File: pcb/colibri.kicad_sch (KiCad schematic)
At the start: 91 parts

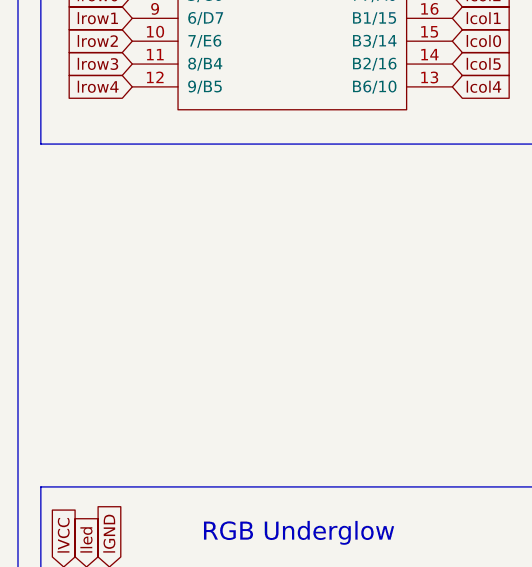
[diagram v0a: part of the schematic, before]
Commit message: TRRS jack in place
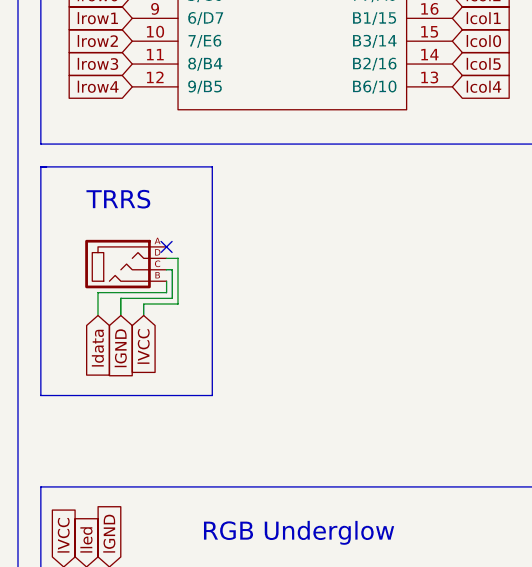
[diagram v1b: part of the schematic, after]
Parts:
- added ljack-1: MJ-4PP-9, kbd:MJ-4PP-9_1side, symbol kbd:MJ-4PP-9
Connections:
- net lGND: now also ljack-1.C
- net lVCC: now also ljack-1.D
- net ldata: now also ljack-1.B
- no-connect marks 7 -> 8
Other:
- note added: "TRRS"
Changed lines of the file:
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@@
   (no_connect (at 35.56 54.61))
   (no_connect (at 71.12 54.61))
+  (no_connect (at 39.37 90.17))
   (wire (pts (xy 163.83 78.74) (xy 163.83 91.44))
     (stroke (width 0) (type default) (color 0 0 0 0))
@@
     (stroke (width 0) (type default) (color 0 0 0 0))
   )
+  (wire (pts (xy 40.005 95.885) (xy 34.29 95.885))
+    (stroke (width 0) (type default) (color 0 0 0 0))
+  )
   (wire (pts (xy 130.81 53.34) (xy 130.81 66.04))
     (stroke (width 0) (type default) (color 0 0 0 0))
@@
     (stroke (width 0) (type default) (color 0 0 0 0))
   )
+  (wire (pts (xy 40.64 91.44) (xy 40.64 96.52))
+    (stroke (width 0) (type default) (color 0 0 0 0))
+  )
   (wire (pts (xy 154.94 68.58) (xy 154.94 72.39))
     (stroke (width 0) (type default) (color 0 0 0 0))
@@
   (wire (pts (xy 39.37 143.51) (xy 39.37 144.78))
     (stroke (width 0) (type default) (color 0 0 0 0))
+  )
+  (polyline (pts (xy 44.45 106.68) (xy 25.4 106.68))
+    (stroke (width 0) (type solid) (color 0 0 0 0))
   )
   (wire (pts (xy 177.8 149.86) (xy 177.8 165.1))
@@
     (stroke (width 0) (type solid) (color 0 0 0 0))
   )
+  (wire (pts (xy 40.64 96.52) (xy 36.83 96.52))
+    (stroke (width 0) (type default) (color 0 0 0 0))
+  )
   (wire (pts (xy 142.24 195.58) (xy 143.51 195.58))
     (stroke (width 0) (type default) (color 0 0 0 0))
   )
+  (polyline (pts (xy 25.4 81.28) (xy 44.45 81.28))
+    (stroke (width 0) (type solid) (color 0 0 0 0))
+  )
   (wire (pts (xy 179.07 66.04) (xy 179.07 68.58))
     (stroke (width 0) (type default) (color 0 0 0 0))
@@
     (stroke (width 0) (type default) (color 0 0 0 0))
   )
+  (wire (pts (xy 39.37 93.98) (xy 39.37 95.25))
+    (stroke (width 0) (type default) (color 0 0 0 0))
+  )
   (wire (pts (xy 171.45 59.69) (xy 187.96 59.69))
     (stroke (width 0) (type default) (color 0 0 0 0))
+  )
+  (polyline (pts (xy 44.45 81.28) (xy 44.45 106.68))
+    (stroke (width 0) (type solid) (color 0 0 0 0))
   )
   (wire (pts (xy 160.02 165.1) (xy 160.02 180.34))
@@
     (stroke (width 0) (type default) (color 0 0 0 0))
   )
+  (polyline (pts (xy 25.4 81.28) (xy 26.035 81.28))
+    (stroke (width 0) (type default) (color 0 0 0 0))
+  )
   (wire (pts (xy 138.43 72.39) (xy 154.94 72.39))
     (stroke (width 0) (type default) (color 0 0 0 0))
@@
     (stroke (width 0) (type solid) (color 0 0 0 0))
   )
+  (polyline (pts (xy 25.4 106.68) (xy 25.4 81.28))
+    (stroke (width 0) (type solid) (color 0 0 0 0))
+  )
   (polyline (pts (xy 85.09 33.02) (xy 85.09 114.3))
     (stroke (width 0) (type solid) (color 0 0 0 0))
@@
     (stroke (width 0) (type default) (color 0 0 0 0))
   )
+  (wire (pts (xy 34.29 95.885) (xy 34.29 97.79))
+    (stroke (width 0) (type default) (color 0 0 0 0))
+  )
   (wire (pts (xy 158.75 165.1) (xy 160.02 165.1))
     (stroke (width 0) (type default) (color 0 0 0 0))
@@
     (stroke (width 0) (type default) (color 0 0 0 0))
   )
+  (wire (pts (xy 39.37 91.44) (xy 40.64 91.44))
+    (stroke (width 0) (type default) (color 0 0 0 0))
+  )
   (wire (pts (xy 106.68 165.1) (xy 107.95 165.1))
     (stroke (width 0) (type default) (color 0 0 0 0))
@@
   )
   (wire (pts (xy 154.94 59.69) (xy 171.45 59.69))
+    (stroke (width 0) (type default) (color 0 0 0 0))
+  )
+  (wire (pts (xy 40.005 92.71) (xy 40.005 95.885))
     (stroke (width 0) (type default) (color 0 0 0 0))
   )
@@
     (stroke (width 0) (type default) (color 0 0 0 0))
   )
+  (wire (pts (xy 31.75 95.25) (xy 31.75 97.79))
+    (stroke (width 0) (type default) (color 0 0 0 0))
+  )
   (wire (pts (xy 124.46 149.86) (xy 125.73 149.86))
     (stroke (width 0) (type default) (color 0 0 0 0))
@@
     (stroke (width 0) (type default) (color 0 0 0 0))
   )
+  (wire (pts (xy 39.37 95.25) (xy 31.75 95.25))
+    (stroke (width 0) (type default) (color 0 0 0 0))
+  )
   (wire (pts (xy 123.19 180.34) (xy 124.46 180.34))
     (stroke (width 0) (type default) (color 0 0 0 0))
   )
   (wire (pts (xy 171.45 68.58) (xy 171.45 72.39))
+    (stroke (width 0) (type default) (color 0 0 0 0))
+  )
+  (wire (pts (xy 39.37 92.71) (xy 40.005 92.71))
     (stroke (width 0) (type default) (color 0 0 0 0))
   )
@@
     (stroke (width 0) (type default) (color 0 0 0 0))
   )
+  (wire (pts (xy 36.83 96.52) (xy 36.83 97.79))
+    (stroke (width 0) (type default) (color 0 0 0 0))
+  )
   (wire (pts (xy 39.37 144.78) (xy 39.37 146.05))
     (stroke (width 0) (type default) (color 0 0 0 0))
@@
   (wire (pts (xy 130.81 91.44) (xy 130.81 104.14))
     (stroke (width 0) (type default) (color 0 0 0 0))
+  )
+  (text "TRRS" (at 30.48 86.36 0)
+    (effects (font (size 2 2)) (justify left bottom))
   )
   (text "SWITCHES" (at 134.62 38.1 0)
@@
     )
   )
+  (global_label "lVCC" (shape input) (at 36.83 97.79 270) (fields_autoplaced)
+    (effects (font (size 1.27 1.27)) (justify right))
+    (property "Intersheet References" "${INTERSHEET_REFS}" (id 0) (at 36.9094 104.4969 90)
+      (effects (font (size 1.27 1.27)) (justify right) hide)
+    )
+  )
   (global_label "lVCC" (shape input) (at 160.02 127 90) (fields_autoplaced)
     (effects (font (size 1.27 1.27)) (justify left))
@@
     )
   )
+  (global_label "ldata" (shape input) (at 31.75 97.79 270) (fields_autoplaced)
+    (effects (font (size 1.27 1.27)) (justify right))
+    (property "Intersheet References" "${INTERSHEET_REFS}" (id 0) (at 31.6706 105.0412 90)
+      (effects (font (size 1.27 1.27)) (justify right) hide)
+    )
+  )
   (global_label "lcol2" (shape input) (at 130.81 46.99 90) (fields_autoplaced)
     (effects (font (size 1.27 1.27)) (justify left))
@@
     )
   )
+  (global_label "lGND" (shape input) (at 34.29 97.79 270) (fields_autoplaced)
+    (effects (font (size 1.27 1.27)) (justify right))
+    (property "Intersheet References" "${INTERSHEET_REFS}" (id 0) (at 34.2106 104.7388 90)
+      (effects (font (size 1.27 1.27)) (justify right) hide)
+    )
+  )
   (global_label "lcol4" (shape input) (at 71.12 72.39 0) (fields_autoplaced)
     (effects (font (size 1.27 1.27)) (justify left))
@@
     (pin "1")
     (pin "2")
+  )
+  (symbol (lib_id "kbd:MJ-4PP-9") (at 34.29 92.075 0) (unit 1)
+    (in_bom yes) (on_board yes)
+    (property "Reference" "ljack-1" (id 0) (at 38.1 87.63 0)
+      (effects (font (size 1.27 1.27)) (justify right) hide)
+    )
+    (property "Value" "MJ-4PP-9" (id 1) (at 33.9725 86.995 0)
+      (effects (font (size 1.27 1.27)) hide)
+    )
+    (property "Footprint" "kbd:MJ-4PP-9_1side" (id 2) (at 41.275 87.63 0)
+      (effects (font (size 1.27 1.27)) hide)
+    )
+    (property "Datasheet" "~" (id 3) (at 41.275 87.63 0)
+      (effects (font (size 1.27 1.27)) hide)
+    )
+    (pin "A")
+    (pin "B")
+    (pin "C")
+    (pin "D")
   )
   (symbol (lib_id "kbd:SW_PUSH") (at 171.45 91.44 0) (unit 1)
@@
       (reference "ld-28") (unit 1) (value "1N4148W") (footprint "kbd:D3_SMD_v2")
     )
+    (path "/17a58034-d3db-4b2b-a530-114b7d872836"
+      (reference "ljack-1") (unit 1) (value "MJ-4PP-9") (footprint "kbd:MJ-4PP-9_1side")
+    )
     (path "/c8613400-5414-468d-9229-e822c0f7d70d"

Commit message: reset button
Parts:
- added lreset-1: SW_PUSH, kbd:ResetSW_4P, symbol kbd:SW_PUSH
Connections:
- net lGND: now also lreset-1.2
- net lreset: now also lreset-1.1
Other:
- note added: "Reset"
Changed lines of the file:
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@@
   (no_connect (at 35.56 54.61))
   (no_connect (at 71.12 54.61))
-  (no_connect (at 39.37 90.17))
+  (no_connect (at 39.37 92.075))
   (wire (pts (xy 163.83 78.74) (xy 163.83 91.44))
     (stroke (width 0) (type default) (color 0 0 0 0))
@@
     (stroke (width 0) (type default) (color 0 0 0 0))
   )
-  (wire (pts (xy 40.005 95.885) (xy 34.29 95.885))
+  (wire (pts (xy 40.005 97.79) (xy 34.29 97.79))
     (stroke (width 0) (type default) (color 0 0 0 0))
   )
@@
     (stroke (width 0) (type default) (color 0 0 0 0))
   )
-  (wire (pts (xy 40.64 91.44) (xy 40.64 96.52))
+  (wire (pts (xy 40.64 93.345) (xy 40.64 98.425))
     (stroke (width 0) (type default) (color 0 0 0 0))
   )
@@
     (stroke (width 0) (type default) (color 0 0 0 0))
   )
-  (polyline (pts (xy 44.45 106.68) (xy 25.4 106.68))
+  (polyline (pts (xy 44.45 107.95) (xy 25.4 107.95))
     (stroke (width 0) (type solid) (color 0 0 0 0))
   )
@@
     (stroke (width 0) (type solid) (color 0 0 0 0))
   )
-  (wire (pts (xy 40.64 96.52) (xy 36.83 96.52))
+  (wire (pts (xy 40.64 98.425) (xy 36.83 98.425))
     (stroke (width 0) (type default) (color 0 0 0 0))
   )
@@
     (stroke (width 0) (type default) (color 0 0 0 0))
   )
+  (polyline (pts (xy 69.85 107.95) (xy 46.99 107.95))
+    (stroke (width 0) (type solid) (color 0 0 0 0))
+  )
   (wire (pts (xy 176.53 134.62) (xy 177.8 134.62))
     (stroke (width 0) (type default) (color 0 0 0 0))
@@
     (stroke (width 0) (type default) (color 0 0 0 0))
   )
-  (wire (pts (xy 39.37 93.98) (xy 39.37 95.25))
+  (wire (pts (xy 39.37 95.885) (xy 39.37 97.155))
     (stroke (width 0) (type default) (color 0 0 0 0))
   )
@@
     (stroke (width 0) (type default) (color 0 0 0 0))
   )
-  (polyline (pts (xy 44.45 81.28) (xy 44.45 106.68))
+  (polyline (pts (xy 44.45 81.28) (xy 44.45 107.95))
     (stroke (width 0) (type solid) (color 0 0 0 0))
   )
@@
     (stroke (width 0) (type default) (color 0 0 0 0))
   )
+  (polyline (pts (xy 46.99 81.28) (xy 69.85 81.28))
+    (stroke (width 0) (type solid) (color 0 0 0 0))
+  )
   (wire (pts (xy 124.46 195.58) (xy 125.73 195.58))
     (stroke (width 0) (type default) (color 0 0 0 0))
@@
     (stroke (width 0) (type default) (color 0 0 0 0))
   )
+  (polyline (pts (xy 46.99 107.95) (xy 46.99 81.28))
+    (stroke (width 0) (type solid) (color 0 0 0 0))
+  )
+  (wire (pts (xy 66.04 99.06) (xy 66.04 94.615))
+    (stroke (width 0) (type default) (color 0 0 0 0))
+  )
   (wire (pts (xy 162.56 66.04) (xy 162.56 68.58))
     (stroke (width 0) (type default) (color 0 0 0 0))
@@
     (stroke (width 0) (type solid) (color 0 0 0 0))
   )
-  (polyline (pts (xy 25.4 106.68) (xy 25.4 81.28))
+  (polyline (pts (xy 25.4 107.95) (xy 25.4 81.28))
     (stroke (width 0) (type solid) (color 0 0 0 0))
   )
@@
     (stroke (width 0) (type default) (color 0 0 0 0))
   )
+  (wire (pts (xy 56.515 99.06) (xy 50.8 99.06))
+    (stroke (width 0) (type default) (color 0 0 0 0))
+  )
   (wire (pts (xy 171.45 85.09) (xy 187.96 85.09))
     (stroke (width 0) (type default) (color 0 0 0 0))
@@
     (stroke (width 0) (type default) (color 0 0 0 0))
   )
-  (wire (pts (xy 34.29 95.885) (xy 34.29 97.79))
+  (wire (pts (xy 34.29 97.79) (xy 34.29 99.695))
     (stroke (width 0) (type default) (color 0 0 0 0))
   )
@@
     (stroke (width 0) (type default) (color 0 0 0 0))
   )
-  (wire (pts (xy 39.37 91.44) (xy 40.64 91.44))
+  (wire (pts (xy 39.37 93.345) (xy 40.64 93.345))
     (stroke (width 0) (type default) (color 0 0 0 0))
   )
@@
     (stroke (width 0) (type default) (color 0 0 0 0))
   )
-  (wire (pts (xy 40.005 92.71) (xy 40.005 95.885))
+  (wire (pts (xy 40.005 94.615) (xy 40.005 97.79))
     (stroke (width 0) (type default) (color 0 0 0 0))
   )
@@
     (stroke (width 0) (type default) (color 0 0 0 0))
   )
-  (wire (pts (xy 31.75 95.25) (xy 31.75 97.79))
+  (wire (pts (xy 31.75 97.155) (xy 31.75 99.695))
     (stroke (width 0) (type default) (color 0 0 0 0))
   )
@@
     (stroke (width 0) (type default) (color 0 0 0 0))
   )
-  (wire (pts (xy 39.37 95.25) (xy 31.75 95.25))
+  (wire (pts (xy 39.37 97.155) (xy 31.75 97.155))
+    (stroke (width 0) (type default) (color 0 0 0 0))
+  )
+  (wire (pts (xy 59.69 99.06) (xy 66.04 99.06))
     (stroke (width 0) (type default) (color 0 0 0 0))
   )
@@
     (stroke (width 0) (type default) (color 0 0 0 0))
   )
-  (wire (pts (xy 39.37 92.71) (xy 40.005 92.71))
+  (wire (pts (xy 39.37 94.615) (xy 40.005 94.615))
     (stroke (width 0) (type default) (color 0 0 0 0))
   )
@@
     (stroke (width 0) (type default) (color 0 0 0 0))
   )
-  (wire (pts (xy 36.83 96.52) (xy 36.83 97.79))
+  (wire (pts (xy 36.83 98.425) (xy 36.83 99.695))
     (stroke (width 0) (type default) (color 0 0 0 0))
   )
@@
   (wire (pts (xy 124.46 165.1) (xy 125.73 165.1))
     (stroke (width 0) (type default) (color 0 0 0 0))
+  )
+  (wire (pts (xy 50.8 99.06) (xy 50.8 94.615))
+    (stroke (width 0) (type default) (color 0 0 0 0))
+  )
+  (polyline (pts (xy 69.85 81.28) (xy 69.85 107.95))
+    (stroke (width 0) (type solid) (color 0 0 0 0))
   )
   (wire (pts (xy 69.85 143.51) (xy 69.85 144.78))
@@
   (text "RGB Underglow" (at 64.77 123.19 180)
     (effects (font (size 2 2)) (justify right bottom))
+  )
+  (text "Reset" (at 53.975 86.36 0)
+    (effects (font (size 2 2)) (justify left bottom))
   )
   (global_label "lcol3" (shape input) (at 71.12 59.69 0) (fields_autoplaced)
@@
     )
   )
-  (global_label "lVCC" (shape input) (at 36.83 97.79 270) (fields_autoplaced)
+  (global_label "lVCC" (shape input) (at 36.83 99.695 270) (fields_autoplaced)
     (effects (font (size 1.27 1.27)) (justify right))
-    (property "Intersheet References" "${INTERSHEET_REFS}" (id 0) (at 36.9094 104.4969 90)
+    (property "Intersheet References" "${INTERSHEET_REFS}" (id 0) (at 36.9094 106.4019 90)
       (effects (font (size 1.27 1.27)) (justify right) hide)
     )
@@
     )
   )
-  (global_label "ldata" (shape input) (at 31.75 97.79 270) (fields_autoplaced)
+  (global_label "ldata" (shape input) (at 31.75 99.695 270) (fields_autoplaced)
     (effects (font (size 1.27 1.27)) (justify right))
-    (property "Intersheet References" "${INTERSHEET_REFS}" (id 0) (at 31.6706 105.0412 90)
+    (property "Intersheet References" "${INTERSHEET_REFS}" (id 0) (at 31.6706 106.9462 90)
       (effects (font (size 1.27 1.27)) (justify right) hide)
     )
@@
     )
   )
+  (global_label "lGND" (shape input) (at 59.69 99.06 270) (fields_autoplaced)
+    (effects (font (size 1.27 1.27)) (justify right))
+    (property "Intersheet References" "${INTERSHEET_REFS}" (id 0) (at 59.7694 106.0088 90)
+      (effects (font (size 1.27 1.27)) (justify right) hide)
+    )
+  )
   (global_label "ldata" (shape input) (at 35.56 46.99 180) (fields_autoplaced)
     (effects (font (size 1.27 1.27)) (justify right))
@@
     )
   )
-  (global_label "lGND" (shape input) (at 34.29 97.79 270) (fields_autoplaced)
+  (global_label "lGND" (shape input) (at 34.29 99.695 270) (fields_autoplaced)
     (effects (font (size 1.27 1.27)) (justify right))
-    (property "Intersheet References" "${INTERSHEET_REFS}" (id 0) (at 34.2106 104.7388 90)
+    (property "Intersheet References" "${INTERSHEET_REFS}" (id 0) (at 34.2106 106.6438 90)
+      (effects (font (size 1.27 1.27)) (justify right) hide)
+    )
+  )
+  (global_label "lreset" (shape input) (at 56.515 99.06 270) (fields_autoplaced)
+    (effects (font (size 1.27 1.27)) (justify right))
+    (property "Intersheet References" "${INTERSHEET_REFS}" (id 0) (at 56.5944 106.8555 90)
       (effects (font (size 1.27 1.27)) (justify right) hide)
     )
@@
     (pin "2")
   )
-  (symbol (lib_id "kbd:MJ-4PP-9") (at 34.29 92.075 0) (unit 1)
-    (in_bom yes) (on_board yes)
-    (property "Reference" "ljack-1" (id 0) (at 38.1 87.63 0)
-      (effects (font (size 1.27 1.27)) (justify right) hide)
-    )
-    (property "Value" "MJ-4PP-9" (id 1) (at 33.9725 86.995 0)
-      (effects (font (size 1.27 1.27)) hide)
-    )
-    (property "Footprint" "kbd:MJ-4PP-9_1side" (id 2) (at 41.275 87.63 0)
-      (effects (font (size 1.27 1.27)) hide)
-    )
-    (property "Datasheet" "~" (id 3) (at 41.275 87.63 0)
+  (symbol (lib_id "kbd:MJ-4PP-9") (at 34.29 93.98 0) (unit 1)
+    (in_bom yes) (on_board yes)
+    (property "Reference" "ljack-1" (id 0) (at 38.1 89.535 0)
+      (effects (font (size 1.27 1.27)) (justify right))
+    )
+    (property "Value" "MJ-4PP-9" (id 1) (at 33.9725 88.9 0)
+      (effects (font (size 1.27 1.27)) hide)
+    )
+    (property "Footprint" "kbd:MJ-4PP-9_1side" (id 2) (at 41.275 89.535 0)
+      (effects (font (size 1.27 1.27)) hide)
+    )
+    (property "Datasheet" "~" (id 3) (at 41.275 89.535 0)
       (effects (font (size 1.27 1.27)) hide)
     )
@@
     (pin "3")
     (pin "4")
+  )
+  (symbol (lib_id "kbd:SW_PUSH") (at 58.42 94.615 0) (unit 1)
+    (in_bom yes) (on_board yes) (fields_autoplaced)
+    (property "Reference" "lreset-1" (id 0) (at 58.42 89.535 0))
+    (property "Value" "SW_PUSH" (id 1) (at 58.42 89.535 0)
+      (effects (font (size 1.27 1.27)) hide)
+    )
+    (property "Footprint" "kbd:ResetSW_4P" (id 2) (at 58.42 94.615 0)
+      (effects (font (size 1.27 1.27)) hide)
+    )
+    (property "Datasheet" "" (id 3) (at 58.42 94.615 0))
+    (pin "1")
+    (pin "2")
   )
   (symbol (lib_id "kbd:YS-SK6812MINI-E") (at 133.35 165.1 90) (unit 1)
@@
       (reference "lled-28") (unit 1) (value "YS-SK6812MINI-E") (footprint "kbd:YS-SK6812MINI-E")
     )
+    (path "/f45bfb45-f489-4e83-ba10-e93859f41fe6"
+      (reference "lreset-1") (unit 1) (value "SW_PUSH") (footprint "kbd:ResetSW_4P")
+    )
     (path "/377a23d8-2fa5-459f-9dad-5a649e830e53"
